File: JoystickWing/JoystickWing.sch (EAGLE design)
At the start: 12 parts, among them J1 5747844-4

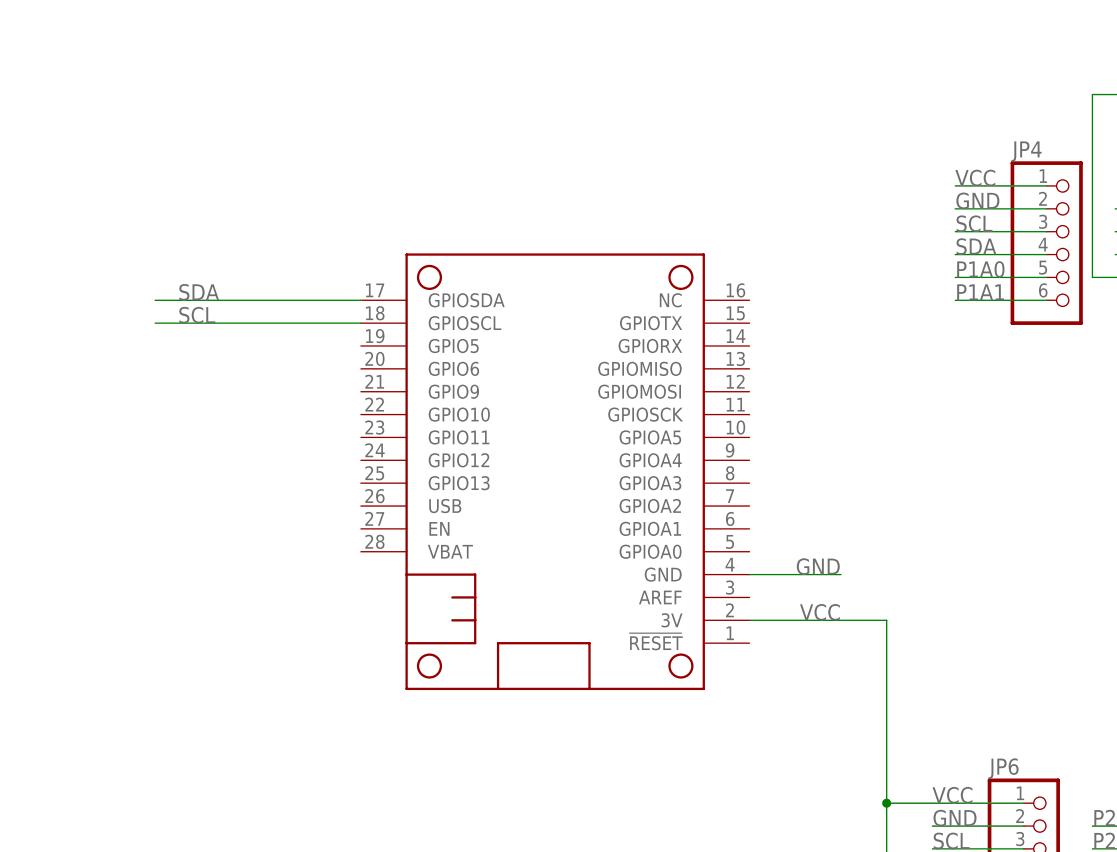
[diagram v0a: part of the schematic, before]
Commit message: Added NeoPixel w/jumper & pin
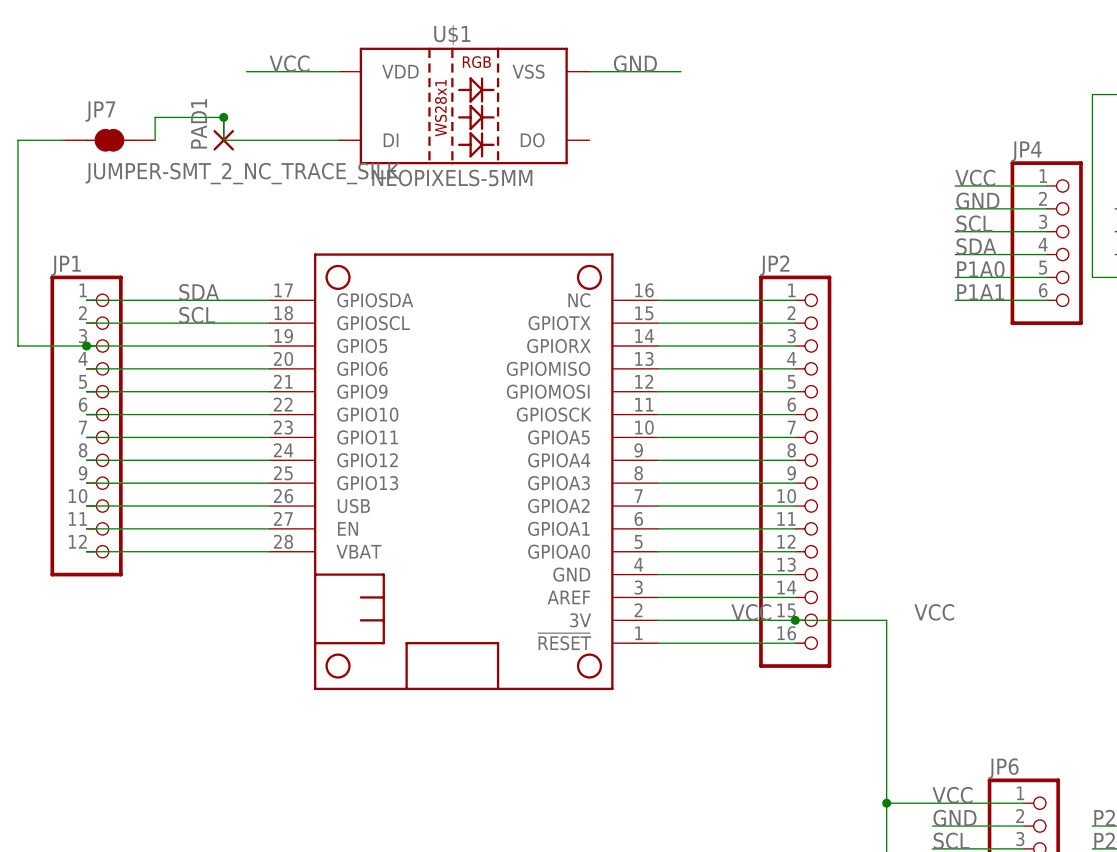
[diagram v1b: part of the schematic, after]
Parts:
- added JP1: (no value), adafruit:PINHD-1X12-CB
- added JP2: (no value), pinhead:PINHD-1X16
- added JP7: JUMPER-SMT_2_NC_TRACE_SILK, SparkFun-Jumpers:JUMPER-SMT_2_NC_TRACE_SILK
- added PAD1: (no value), wirepad:2,54/1,1
- added U$1: NEOPIXELS-5MM, milador:NEOPIXELS-5MM
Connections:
- new net N$1: JP1.3, JP7.1, MS1.GPIO5
- new net N$10: JP2.1, MS1.NC
- new net N$11: JP2.2, MS1.GPIOTX
- new net N$12: JP2.3, MS1.GPIORX
- new net N$13: JP2.4, MS1.GPIOMISO
- new net N$14: JP2.5, MS1.GPIOMOSI
- new net N$15: JP2.6, MS1.GPIOSCK
- new net N$16: JP2.7, MS1.GPIOA5
- new net N$17: JP2.8, MS1.GPIOA4
- new net N$18: JP2.9, MS1.GPIOA3
- new net N$19: JP2.10, MS1.GPIOA2
- new net N$2: JP1.4, MS1.GPIO6
- new net N$20: JP2.11, MS1.GPIOA1
- new net N$21: JP2.12, MS1.GPIOA0
- new net N$22: JP2.13, MS1.GND
- new net N$23: JP2.14, MS1.AREF
- new net N$24: JP2.16, MS1.!RESET
- new net N$25: JP7.2, PAD1.P, U$1.DI
- new net N$3: JP1.5, MS1.GPIO9
- new net N$4: JP1.6, MS1.GPIO10
- new net N$5: JP1.7, MS1.GPIO11
- new net N$6: JP1.8, MS1.GPIO12
- new net N$8: JP1.9, MS1.GPIO13
- new net N$9: JP1.11, MS1.EN
- new net USB: JP1.10, MS1.USB
- new net VBAT: JP1.12, MS1.VBAT
- net GND: now also U$1.VSS; no longer MS1.GND
- net SCL: now also JP1.2
- net SDA: now also JP1.1
- net VCC: now also JP2.15, U$1.VDD
